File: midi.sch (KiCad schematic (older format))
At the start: 3 parts

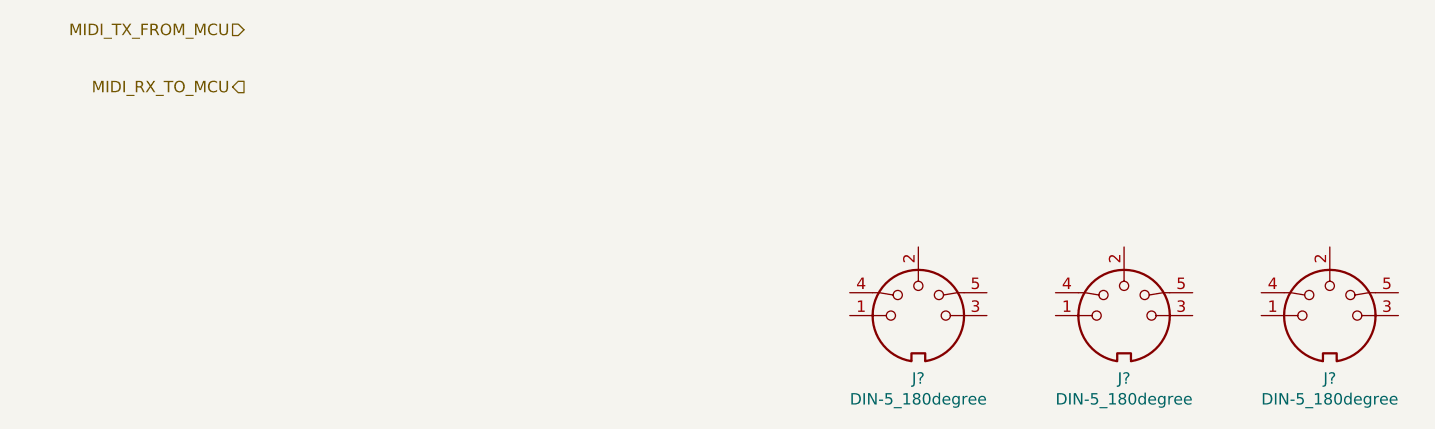
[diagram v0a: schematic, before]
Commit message: Added some footprints. Basic board outline.
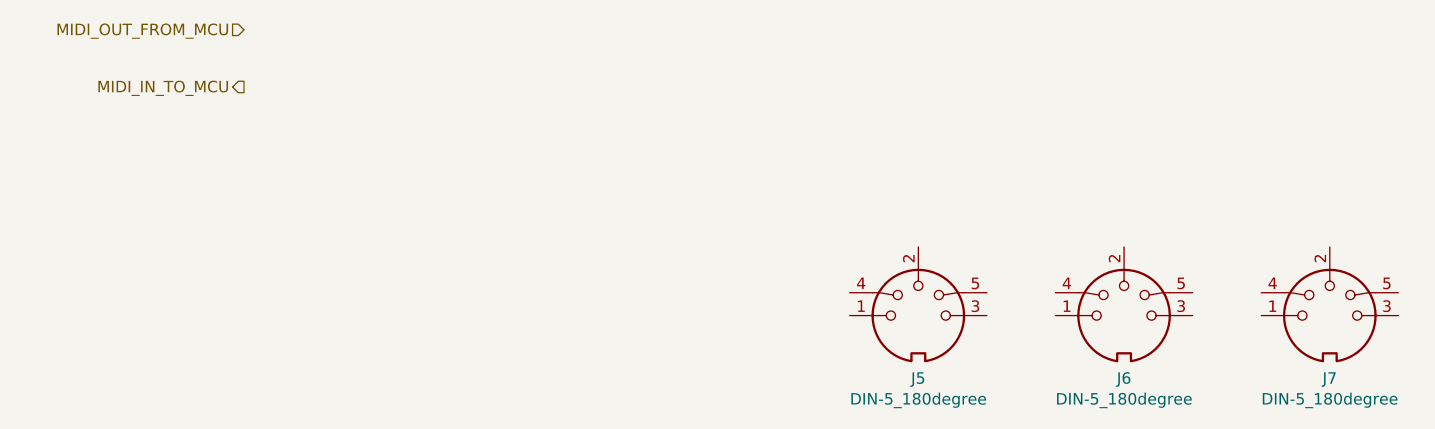
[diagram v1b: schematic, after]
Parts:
- J5, J6, J7: renamed from J?; footprint (none) -> JGP Footprints:5P180 DIN Socket
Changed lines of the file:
@@
 $EndDescr
 Text HLabel 1750 1200 0    50   Input ~ 0
-MIDI_TX_FROM_MCU
+MIDI_OUT_FROM_MCU
 Text HLabel 1750 1450 0    50   Output ~ 0
-MIDI_RX_TO_MCU
+MIDI_IN_TO_MCU
 $Comp
 L Connector:DIN-5_180degree J?
@@
 P 4700 2450
 AR Path="/5DF5386C" Ref="J?"  Part="1"
-AR Path="/5DF253FB/5DF5386C" Ref="J?"  Part="1"
-F 0 "J?" H 4700 2175 50  0000 C CNN
+AR Path="/5DF253FB/5DF5386C" Ref="J5"  Part="1"
+F 0 "J5" H 4700 2175 50  0000 C CNN
 F 1 "DIN-5_180degree" H 4700 2084 50  0000 C CNN
-F 2 "" H 4700 2450 50  0001 C CNN
+F 2 "JGP Footprints:5P180 DIN Socket" H 4700 2450 50  0001 C CNN
 F 3 "http://www.mouser.com/ds/2/18/40_c091_abd_e-75918.pdf" H 4700 2450 50  0001 C CNN
 	1    4700 2450
@@
 P 5600 2450
 AR Path="/5DF53872" Ref="J?"  Part="1"
-AR Path="/5DF253FB/5DF53872" Ref="J?"  Part="1"
-F 0 "J?" H 5600 2175 50  0000 C CNN
+AR Path="/5DF253FB/5DF53872" Ref="J6"  Part="1"
+F 0 "J6" H 5600 2175 50  0000 C CNN
 F 1 "DIN-5_180degree" H 5600 2084 50  0000 C CNN
-F 2 "" H 5600 2450 50  0001 C CNN
+F 2 "JGP Footprints:5P180 DIN Socket" H 5600 2450 50  0001 C CNN
 F 3 "http://www.mouser.com/ds/2/18/40_c091_abd_e-75918.pdf" H 5600 2450 50  0001 C CNN
 	1    5600 2450
@@
 P 6500 2450
 AR Path="/5DF53878" Ref="J?"  Part="1"
-AR Path="/5DF253FB/5DF53878" Ref="J?"  Part="1"
-F 0 "J?" H 6500 2175 50  0000 C CNN
+AR Path="/5DF253FB/5DF53878" Ref="J7"  Part="1"
+F 0 "J7" H 6500 2175 50  0000 C CNN
 F 1 "DIN-5_180degree" H 6500 2084 50  0000 C CNN
-F 2 "" H 6500 2450 50  0001 C CNN
+F 2 "JGP Footprints:5P180 DIN Socket" H 6500 2450 50  0001 C CNN
 F 3 "http://www.mouser.com/ds/2/18/40_c091_abd_e-75918.pdf" H 6500 2450 50  0001 C CNN
 	1    6500 2450

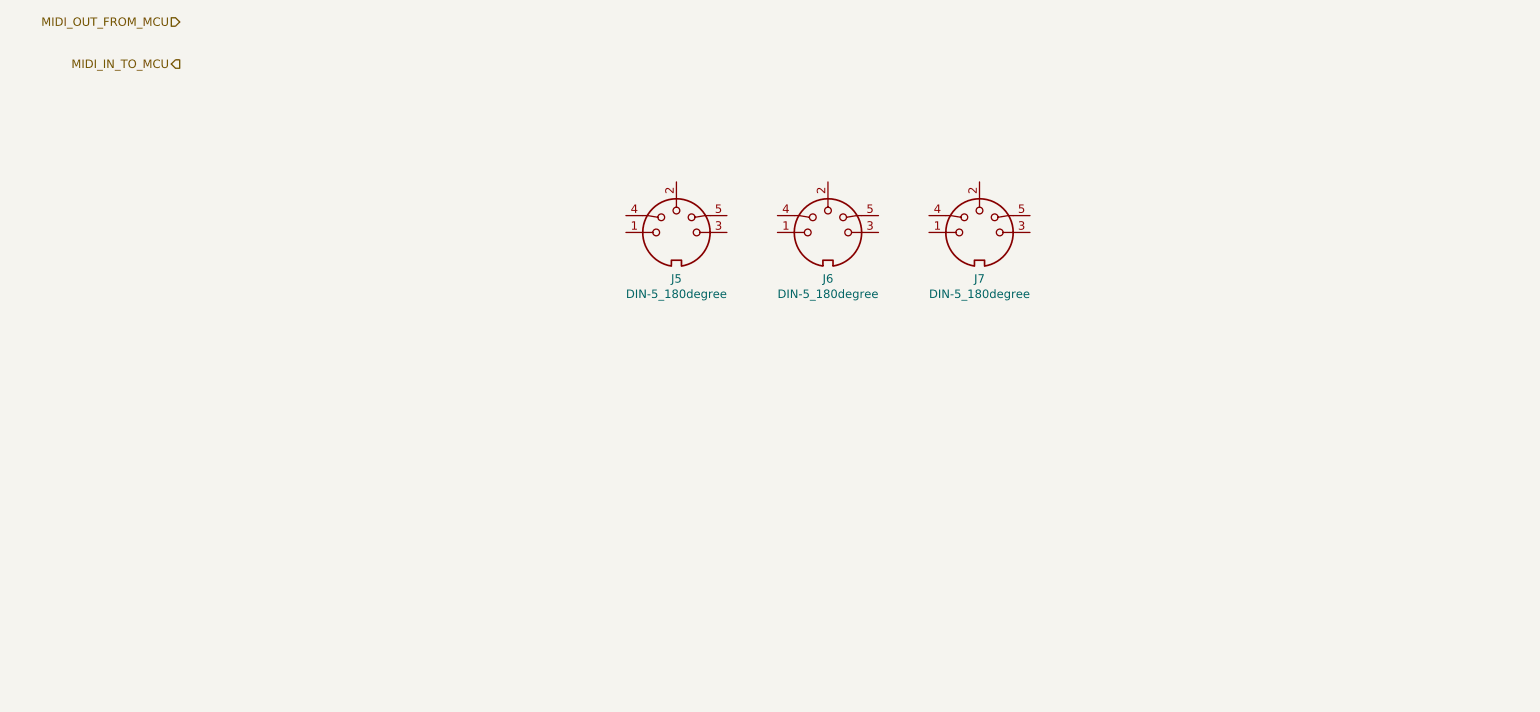
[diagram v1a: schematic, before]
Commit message: Completed Power, SD, MIDI, Parallel and Joystick sheets.
Switch to sheet based 100x part numbering.
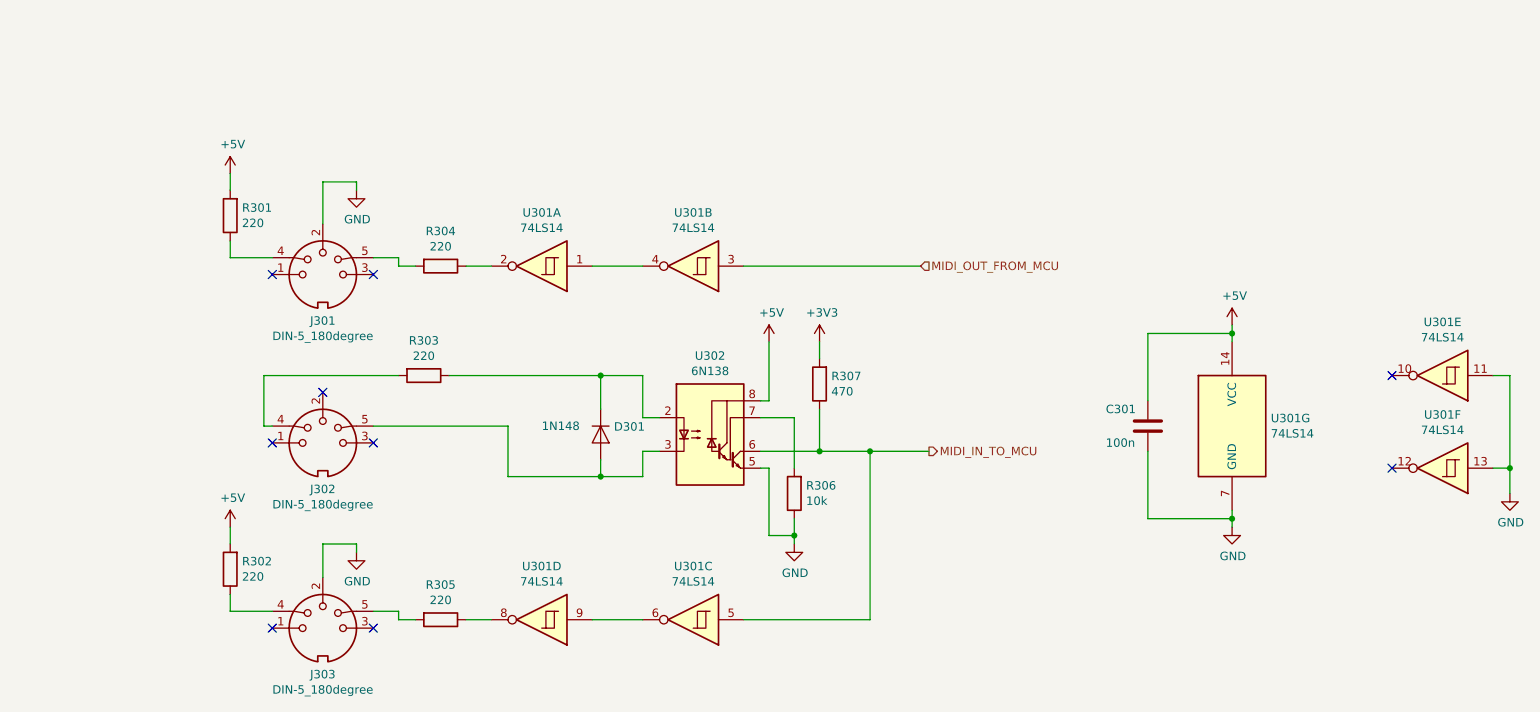
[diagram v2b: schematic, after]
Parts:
- added C301: 100n, symbol Device:C
- added D301: 1N148, symbol Device:D
- added R301, R302, R303, R304, R305: 220, symbol Device:R
- added R306: 10k, symbol Device:R
- added R307: 470, symbol Device:R
- added U301: 74LS14, symbol 74xx:74LS14
- added U302: 6N138, symbol Isolator:6N138
- J302: renamed from J5; RS (none) -> 491-087
- renumbered J6 to J301, J7 to J303
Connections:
- net MIDI_IN_TO_MCU: now also R307.1, U301.5, U302.6 (VO2)
- net MIDI_OUT_FROM_MCU: now also U301.3
- net at J302.4: now also R303.2
- net at J302.5: now also D301.2 (A), U302.3 (C2)
- net GND: now reaches J301.2
- net GND: now also J303.2, C301.2, R306.1, U301.11, U301.13, U301.7 (GND), U302.5 (GND)
- net at J301.4: now also R301.1
- net at J301.5: now also R304.2
- net at J303.4: now also R302.1
- net at J303.5: now also R305.2
- new net: D301.1 (K), R303.1, U302.2 (C1)
- new net: R306.2, U302.7 (VO1)
- new net: U301.1, U301.4
- new net: R304.1, U301.2
- new net: U301.6, U301.9
- new net: R305.1, U301.8
- new net +3V3: R307.2
- new net +5V: C301.1, R301.2, R302.2, U301.14 (VCC), U302.8 (VCC)
- no-connect marks 0 -> 9
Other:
- moved on the sheet: J301, J302, J303

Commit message: Schematic capture draft complete.
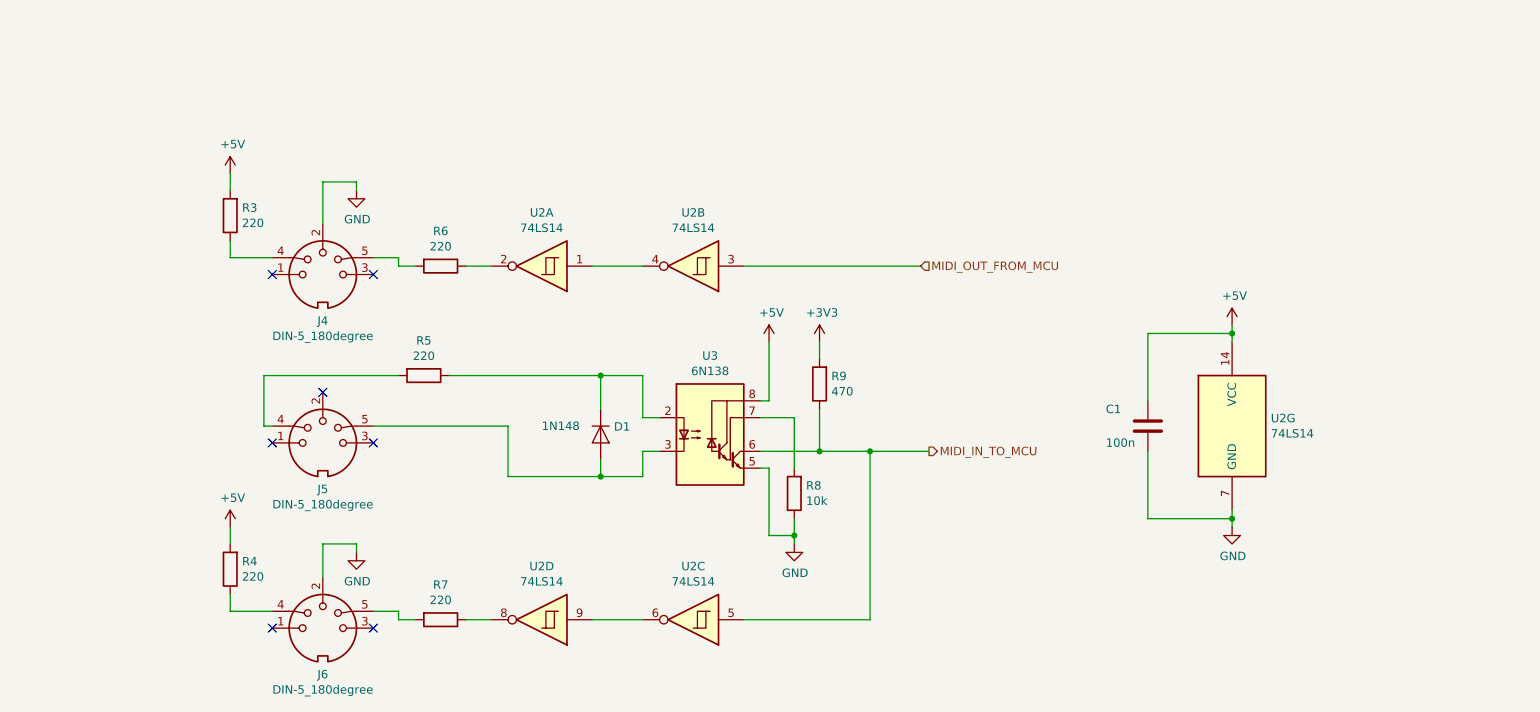
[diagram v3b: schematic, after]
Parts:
- removed unit 5 of U301
- removed unit 6 of U301
- C1: renamed from C301; footprint (none) -> Capacitor_THT:C_Disc_D3.0mm_W2.0mm_P2.50mm
- D1: renamed from D301; footprint (none) -> Diode_THT:D_DO-35_SOD27_P7.62mm_Horizontal
- R3: renamed from R301; footprint (none) -> Resistor_THT:R_Axial_DIN0411_L9.9mm_D3.6mm_P12.70mm_Horizontal
- R4: renamed from R302; footprint (none) -> Resistor_THT:R_Axial_DIN0411_L9.9mm_D3.6mm_P12.70mm_Horizontal
- R5: renamed from R303; footprint (none) -> Resistor_THT:R_Axial_DIN0411_L9.9mm_D3.6mm_P12.70mm_Horizontal
- R6: renamed from R304; footprint (none) -> Resistor_THT:R_Axial_DIN0411_L9.9mm_D3.6mm_P12.70mm_Horizontal
- R7: renamed from R305; footprint (none) -> Resistor_THT:R_Axial_DIN0411_L9.9mm_D3.6mm_P12.70mm_Horizontal
- R8: renamed from R306; footprint (none) -> Resistor_THT:R_Axial_DIN0411_L9.9mm_D3.6mm_P12.70mm_Horizontal
- R9: renamed from R307; footprint (none) -> Resistor_THT:R_Axial_DIN0411_L9.9mm_D3.6mm_P12.70mm_Horizontal
- U2: renamed from U301; footprint (none) -> Package_DIP:DIP-14_W7.62mm
- U3: renamed from U302; footprint (none) -> Package_DIP:DIP-8-16_W7.62mm
- renumbered J301 to J4, J302 to J5, J303 to J6
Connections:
- no-connect marks 9 -> 7

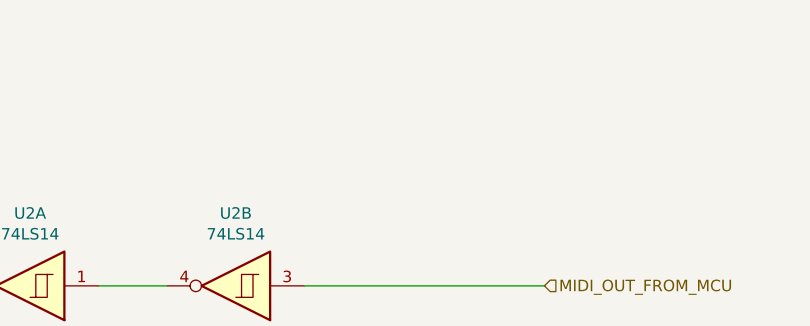
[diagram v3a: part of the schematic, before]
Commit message: Tidied up Atmega power. Added page titles.
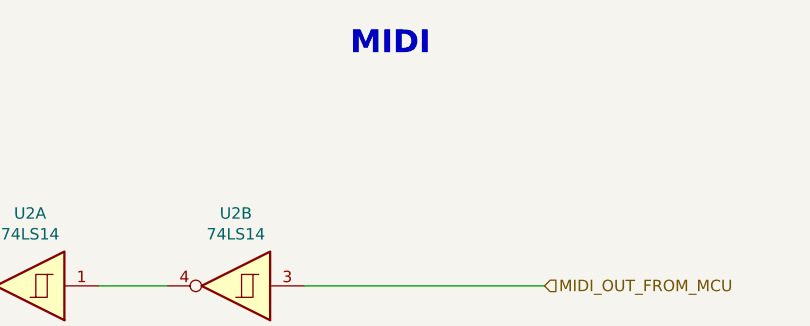
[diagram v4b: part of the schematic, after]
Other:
- note added: "MIDI"
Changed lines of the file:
@@
 Sheet 2 10
 Title "Neotron 32K Main PCB"
-Date "2019-12-15"
-Rev "0.5"
+Date "2019-12-16"
+Rev "0.6"
 Comp "github.com/neotron-compute/Neotron-32-Hardware"
 Comment1 "Copyright (c) Jonathan 'theJPster' Pallant"
@@
 Wire Wire Line
 	2600 2150 2600 2400
+Text Notes 5300 1650 0    100  ~ 20
+MIDI
 $EndSCHEMATC

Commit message: Work in progress.
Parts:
- U3: footprint Package_DIP:DIP-8-16_W7.62mm -> Package_DIP:DIP-8_W7.62mm
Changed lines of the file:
@@
 F 0 "U3" H 4900 4117 50  0000 C CNN
 F 1 "6N138" H 4900 4026 50  0000 C CNN
-F 2 "Package_DIP:DIP-8-16_W7.62mm" H 5190 3350 50  0001 C CNN
+F 2 "Package_DIP:DIP-8_W7.62mm" H 5190 3350 50  0001 C CNN
 F 3 "http://www.onsemi.com/pub/Collateral/HCPL2731-D.pdf" H 5190 3350 50  0001 C CNN
 	1    4900 3650

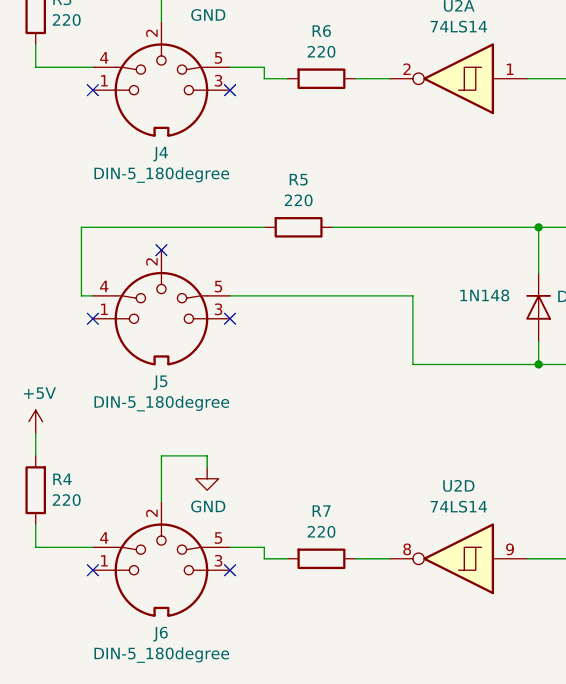
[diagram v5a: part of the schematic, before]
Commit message: Updated footprints: ) Swapped RS-232 DE9 for IDC header. ) Large caps are radial electrolytics. ) Made resistors a little smaller.
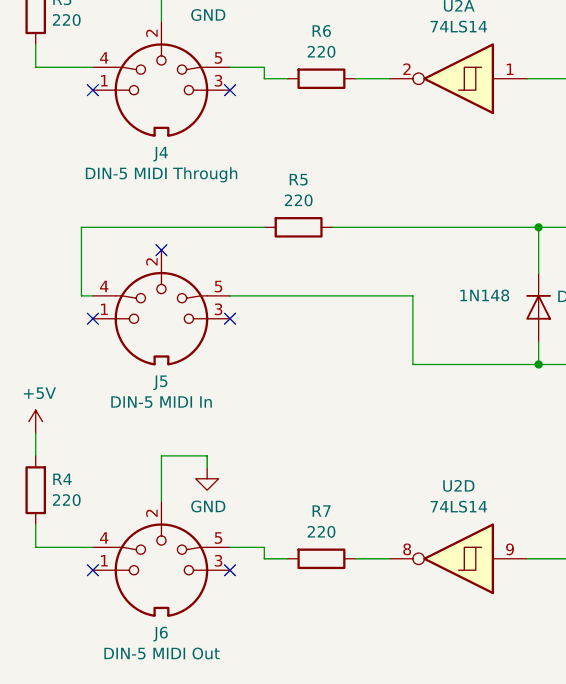
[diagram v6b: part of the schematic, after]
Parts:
- J4: value DIN-5_180degree -> DIN-5 MIDI Through
- J5: value DIN-5_180degree -> DIN-5 MIDI In
- J6: value DIN-5_180degree -> DIN-5 MIDI Out
- R3, R4, R5, R6, R7, R8, R9: footprint Resistor_THT:R_Axial_DIN0411_L9.9mm_D3.6mm_P12.70mm_Horizontal -> Resistor_THT:R_Axial_DIN0207_L6.3mm_D2.5mm_P10.16mm_Horizontal
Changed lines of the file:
@@
 AR Path="/5DF253FB/5DF5386C" Ref="J5"  Part="1"
 F 0 "J5" H 2600 3425 50  0000 C CNN
-F 1 "DIN-5_180degree" H 2600 3334 50  0000 C CNN
+F 1 "DIN-5 MIDI In" H 2600 3334 50  0000 C CNN
 F 2 "JGP Footprints:5P180 DIN Socket" H 2600 3700 50  0001 C CNN
 F 3 "https://docs.rs-online.com/1ee9/0900766b81579be1.pdf" H 2600 3700 50  0001 C CNN
@@
 AR Path="/5DF253FB/5DF53872" Ref="J4"  Part="1"
 F 0 "J4" H 2600 2425 50  0000 C CNN
-F 1 "DIN-5_180degree" H 2600 2334 50  0000 C CNN
+F 1 "DIN-5 MIDI Through" H 2600 2334 50  0000 C CNN
 F 2 "JGP Footprints:5P180 DIN Socket" H 2600 2700 50  0001 C CNN
 F 3 "http://www.mouser.com/ds/2/18/40_c091_abd_e-75918.pdf" H 2600 2700 50  0001 C CNN
@@
 AR Path="/5DF253FB/5DF53878" Ref="J6"  Part="1"
 F 0 "J6" H 2600 4525 50  0000 C CNN
-F 1 "DIN-5_180degree" H 2600 4434 50  0000 C CNN
+F 1 "DIN-5 MIDI Out" H 2600 4434 50  0000 C CNN
 F 2 "JGP Footprints:5P180 DIN Socket" H 2600 4800 50  0001 C CNN
 F 3 "http://www.mouser.com/ds/2/18/40_c091_abd_e-75918.pdf" H 2600 4800 50  0001 C CNN
@@
 F 0 "R5" V 2993 3300 50  0000 C CNN
 F 1 "220" V 3084 3300 50  0000 C CNN
-F 2 "Resistor_THT:R_Axial_DIN0411_L9.9mm_D3.6mm_P12.70mm_Horizontal" V 3130 3300 50  0001 C CNN
+F 2 "Resistor_THT:R_Axial_DIN0207_L6.3mm_D2.5mm_P10.16mm_Horizontal" V 3130 3300 50  0001 C CNN
 F 3 "~" H 3200 3300 50  0001 C CNN
 	1    3200 3300
@@
 F 0 "R6" V 3093 2650 50  0000 C CNN
 F 1 "220" V 3184 2650 50  0000 C CNN
-F 2 "Resistor_THT:R_Axial_DIN0411_L9.9mm_D3.6mm_P12.70mm_Horizontal" V 3230 2650 50  0001 C CNN
+F 2 "Resistor_THT:R_Axial_DIN0207_L6.3mm_D2.5mm_P10.16mm_Horizontal" V 3230 2650 50  0001 C CNN
 F 3 "~" H 3300 2650 50  0001 C CNN
 	1    3300 2650
@@
 F 0 "R7" V 3093 4750 50  0000 C CNN
 F 1 "220" V 3184 4750 50  0000 C CNN
-F 2 "Resistor_THT:R_Axial_DIN0411_L9.9mm_D3.6mm_P12.70mm_Horizontal" V 3230 4750 50  0001 C CNN
+F 2 "Resistor_THT:R_Axial_DIN0207_L6.3mm_D2.5mm_P10.16mm_Horizontal" V 3230 4750 50  0001 C CNN
 F 3 "~" H 3300 4750 50  0001 C CNN
 	1    3300 4750
@@
 F 0 "R9" H 5480 3304 50  0000 R CNN
 F 1 "470" H 5480 3395 50  0000 R CNN
-F 2 "Resistor_THT:R_Axial_DIN0411_L9.9mm_D3.6mm_P12.70mm_Horizontal" V 5480 3350 50  0001 C CNN
+F 2 "Resistor_THT:R_Axial_DIN0207_L6.3mm_D2.5mm_P10.16mm_Horizontal" V 5480 3350 50  0001 C CNN
 F 3 "~" H 5550 3350 50  0001 C CNN
 	1    5550 3350
@@
 F 0 "R8" H 5330 3954 50  0000 R CNN
 F 1 "10k" H 5330 4045 50  0000 R CNN
-F 2 "Resistor_THT:R_Axial_DIN0411_L9.9mm_D3.6mm_P12.70mm_Horizontal" V 5330 4000 50  0001 C CNN
+F 2 "Resistor_THT:R_Axial_DIN0207_L6.3mm_D2.5mm_P10.16mm_Horizontal" V 5330 4000 50  0001 C CNN
 F 3 "~" H 5400 4000 50  0001 C CNN
 	1    5400 4000
@@
 F 0 "R4" H 1980 4404 50  0000 R CNN
 F 1 "220" H 1980 4495 50  0000 R CNN
-F 2 "Resistor_THT:R_Axial_DIN0411_L9.9mm_D3.6mm_P12.70mm_Horizontal" V 1980 4450 50  0001 C CNN
+F 2 "Resistor_THT:R_Axial_DIN0207_L6.3mm_D2.5mm_P10.16mm_Horizontal" V 1980 4450 50  0001 C CNN
 F 3 "~" H 2050 4450 50  0001 C CNN
 	1    2050 4450
@@
 F 0 "R3" H 1980 2304 50  0000 R CNN
 F 1 "220" H 1980 2395 50  0000 R CNN
-F 2 "Resistor_THT:R_Axial_DIN0411_L9.9mm_D3.6mm_P12.70mm_Horizontal" V 1980 2350 50  0001 C CNN
+F 2 "Resistor_THT:R_Axial_DIN0207_L6.3mm_D2.5mm_P10.16mm_Horizontal" V 1980 2350 50  0001 C CNN
 F 3 "~" H 2050 2350 50  0001 C CNN
 	1    2050 2350
